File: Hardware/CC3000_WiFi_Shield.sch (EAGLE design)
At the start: 37 parts, among them J1 U.FL, U2 ARDUINO_SHIELDNOLABELS, U3 74HC4050, U4 USD-SOCKETNEW, U5 CC3000, U6 74AHC1G125

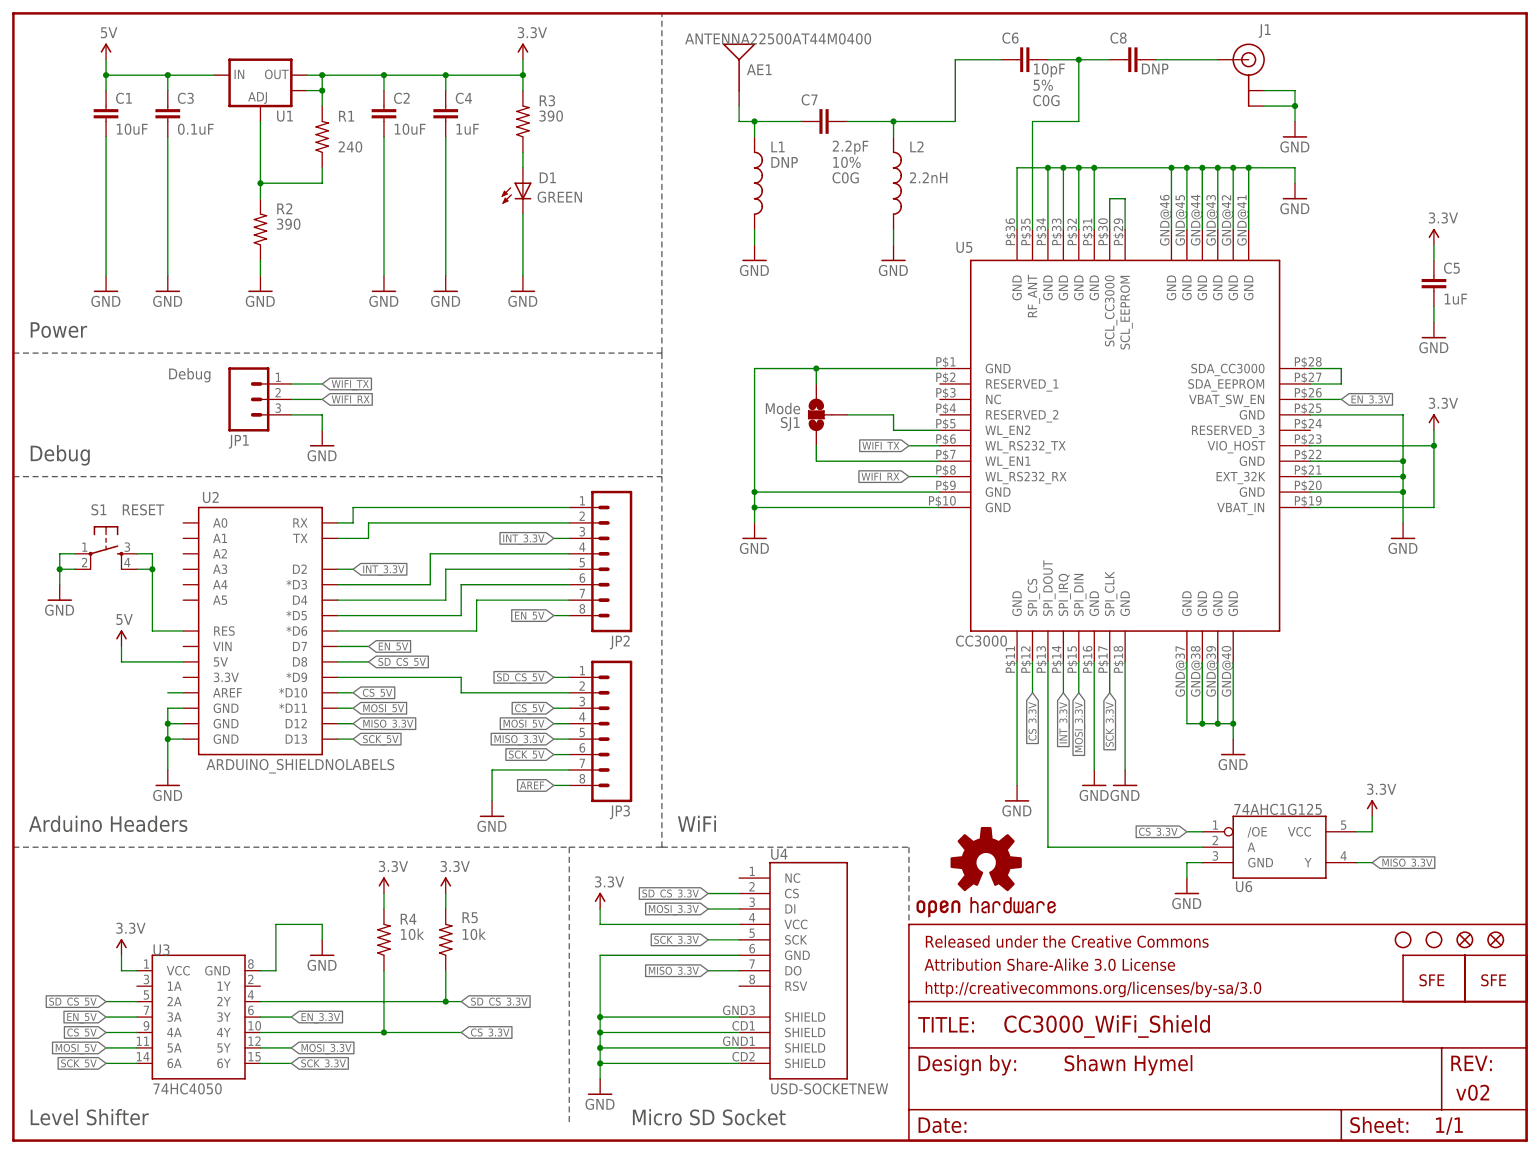
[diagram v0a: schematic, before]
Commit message: Added power breakout near proto area. Removed silk from shield headers. Changed silk text to 0.032 in. size. Added ISP headers to work with Leonardo. Added 10-pin shield headers to work woth UNO R3. Adjusted notch on bottom-right corner of board.
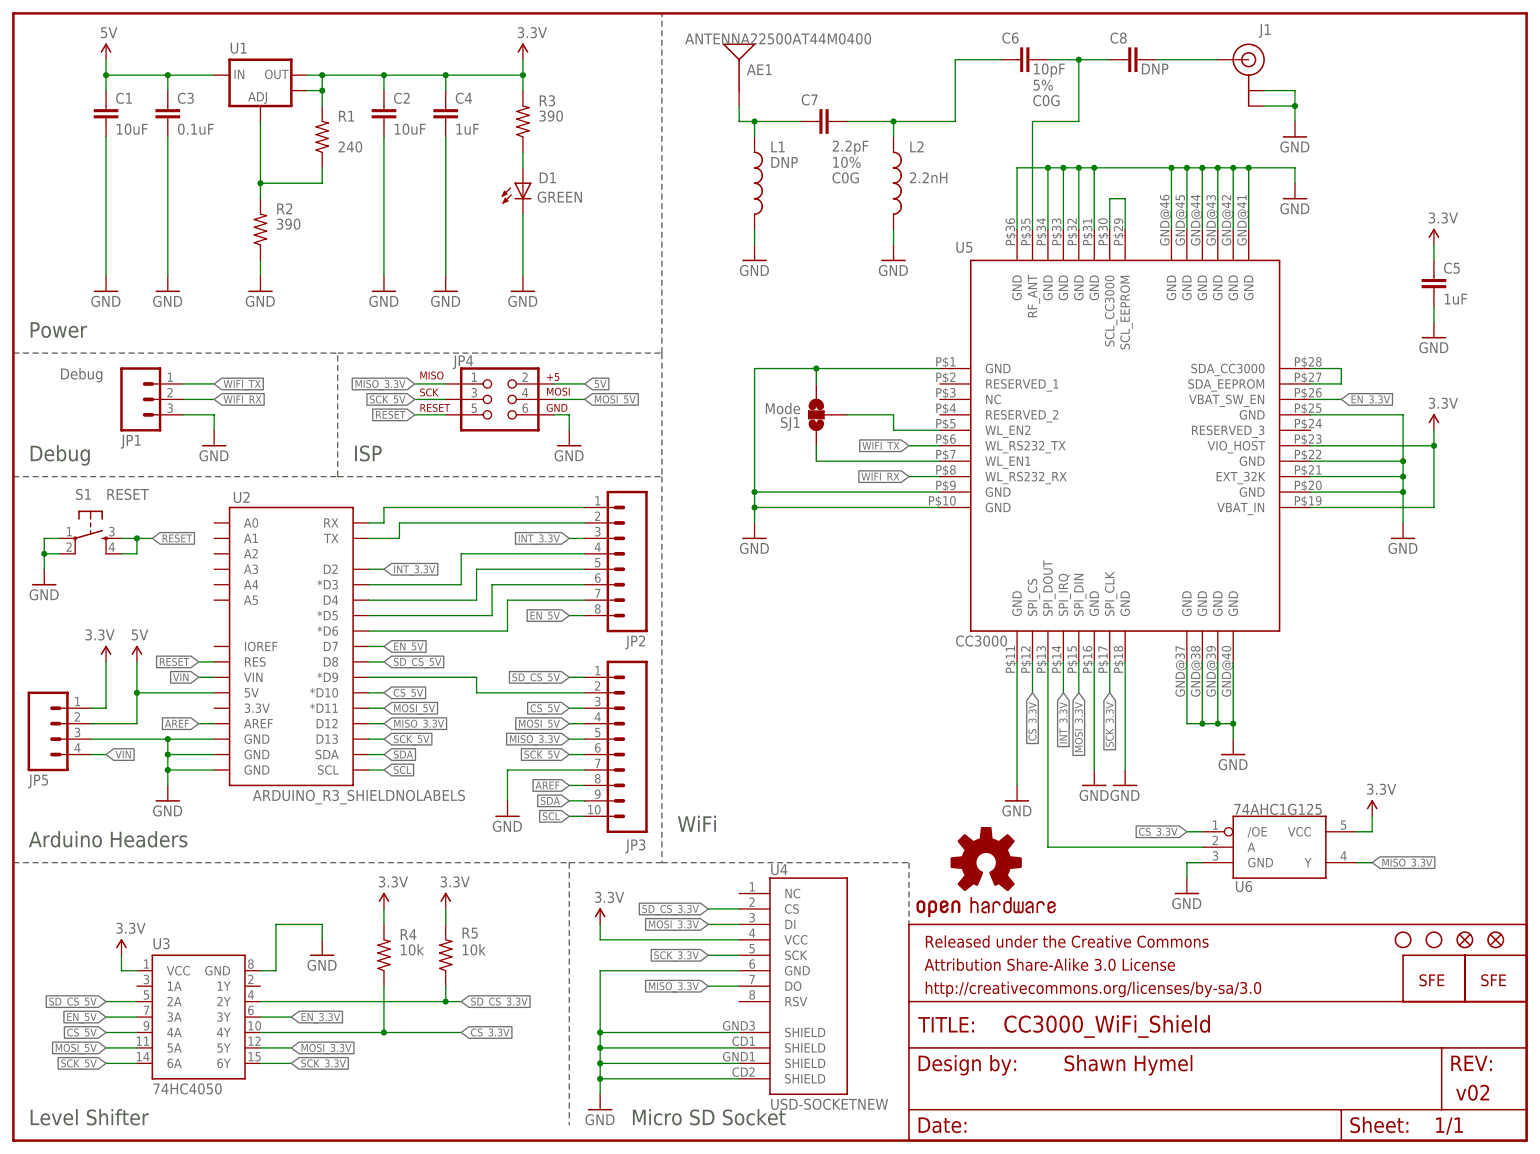
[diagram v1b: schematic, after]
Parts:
- added JP4: AVR_SPI_PRG_6PTH, SparkFun-Connectors:AVR_SPI_PRG_6PTH
- added JP5: (no value), SparkFun-Connectors:M04PTH
- JP2: device SparkFun-Connectors:M081X08 -> SparkFun-Connectors:M08NO_SILK
- JP3: value (none) -> M10NO_SILK; device SparkFun-Connectors:M081X08 -> SparkFun-Connectors:M10NO_SILK
- U2: value ARDUINO_SHIELDNOLABELS -> ARDUINO_R3_SHIELDNOLABELS; device SparkFun-Boards:ARDUINO_SHIELDNOLABELS -> SparkFun-Boards:ARDUINO_R3_SHIELDNOLABELS
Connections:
- removed net N$1: S1.3, S1.4, U2.RES
- new net RESET: JP4.5, S1.3, S1.4, U2.RES
- new net SCL: JP3.10, U2.SCL
- new net SDA: JP3.9, U2.SDA
- new net VIN: JP5.4, U2.VIN
- net 3.3V: now also JP5.1
- net 5V: now also JP4.2, JP5.2
- net GND: now also JP4.6, JP5.3
- net MISO_3.3V: now also JP4.1
- net MOSI_5V: now also JP4.4
- net SCK_5V: now also JP4.3
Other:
- note added: "ISP"
- moved on the sheet: JP1, JP2, R4, R5, S1, U4

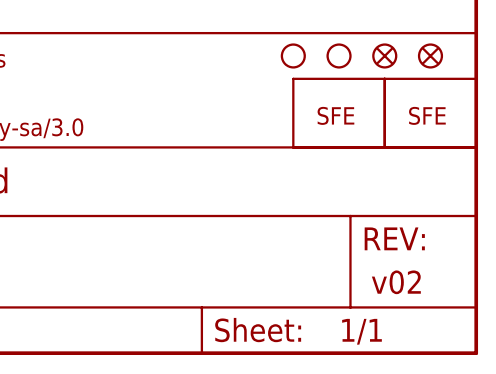
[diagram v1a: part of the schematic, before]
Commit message: Moved ext antenna mount back 50 mil; re-routed SD_CS line to avoid splitting power plane on bottom; Added 'Antenna Select' to SS; Added SS marker to U.FL; Added 'Mode' in SS to jumper; Changed to v10
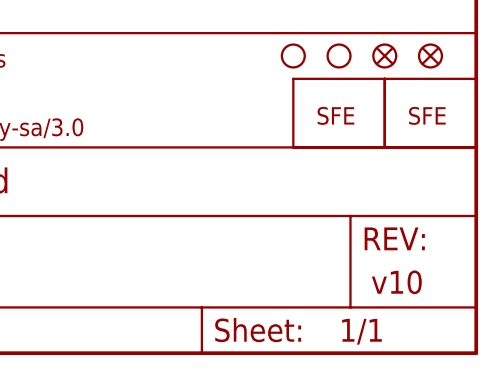
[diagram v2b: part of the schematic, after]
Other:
- note added: "v10"
- note removed: "v02"
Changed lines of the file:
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@@
 <plain>
 <text x="172.72" y="12.7" size="2.54" layer="94" align="center-left">Shawn Hymel</text>
-<text x="237.236" y="6.604" size="2.54" layer="94">v02</text>
+<text x="237.236" y="6.604" size="2.54" layer="94">v10</text>
 <wire x1="0" y1="129.54" x2="53.34" y2="129.54" width="0.1524" layer="97" style="longdash"/>
 <wire x1="53.34" y1="129.54" x2="106.68" y2="129.54" width="0.1524" layer="97" style="longdash"/>

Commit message: Added silk U.FL; Adjusted tvalue markings for easier reading
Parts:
- L1: value (none) -> DNP; PLACE DNP -> (none)
- U1: value (none) -> LM1117
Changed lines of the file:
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@@
 <setting verticaltext="up"/>
 </settings>
-<grid distance="0.1" unitdist="inch" unit="inch" style="lines" multiple="1" display="no" altdistance="0.01" altunitdist="inch" altunit="inch"/>
+<grid distance="0.1" unitdist="inch" unit="inch" style="lines" multiple="1" display="yes" altdistance="0.01" altunitdist="inch" altunit="inch"/>
 <layers>
 <layer number="1" name="Top" color="4" fill="1" visible="no" active="no"/>
@@
 <part name="R1" library="SparkFun-Resistors" deviceset="RESISTOR" device="0603" value="240"/>
 <part name="R2" library="SparkFun-Resistors" deviceset="RESISTOR" device="0603" value="390"/>
-<part name="U1" library="SparkFun-PowerIC" deviceset="V_REG_LM1117" device="SOT223"/>
+<part name="U1" library="SparkFun-PowerIC" deviceset="V_REG_LM1117" device="SOT223" value="LM1117"/>
 <part name="GND1" library="SparkFun-Aesthetics" deviceset="GND" device=""/>
 <part name="GND2" library="SparkFun-Aesthetics" deviceset="GND" device=""/>
@@
 <attribute name="TOL" value="5%"/>
 </part>
-<part name="L1" library="SparkFun-Passives" deviceset="INDUCTOR" device="0603">
-<attribute name="PLACE" value="DNP"/>
-</part>
+<part name="L1" library="SparkFun-Passives" deviceset="INDUCTOR" device="0603" value="DNP"/>
 <part name="L2" library="SparkFun-Passives" deviceset="INDUCTOR" device="0603" value="2.2nH"/>
 <part name="GND15" library="SparkFun-Aesthetics" deviceset="GND" device=""/>
@@
 <instance part="U1" gate="G$1" x="40.64" y="175.26" smashed="yes">
 <attribute name="NAME" x="35.56" y="178.816" size="1.778" layer="95"/>
-<attribute name="VALUE" x="35.56" y="179.07" size="1.778" layer="96"/>
+<attribute name="VALUE" x="40.64" y="179.07" size="1.778" layer="96"/>
 </instance>
 <instance part="GND1" gate="1" x="40.64" y="139.7"/>
@@
 <attribute name="VALUE" x="167.64" y="175.387" size="1.778" layer="96"/>
 </instance>
-<instance part="L1" gate="G$1" x="121.92" y="157.48">
-<attribute name="PLACE" x="124.46" y="160.02" size="1.778" layer="96"/>
+<instance part="L1" gate="G$1" x="121.92" y="157.48" smashed="yes">
+<attribute name="NAME" x="124.46" y="162.56" size="1.778" layer="95"/>
+<attribute name="VALUE" x="124.46" y="160.02" size="1.778" layer="96"/>
 </instance>
 <instance part="L2" gate="G$1" x="144.78" y="157.48" smashed="yes">
